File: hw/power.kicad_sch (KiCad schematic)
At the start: 22 parts, among them J2 USB_C_Receptacle_USB2.0_16P, J3 Conn_01x02_Pin, U3 TPD2EUSB30A, U4 BQ24075RGT, U5 TPS63020DSJR

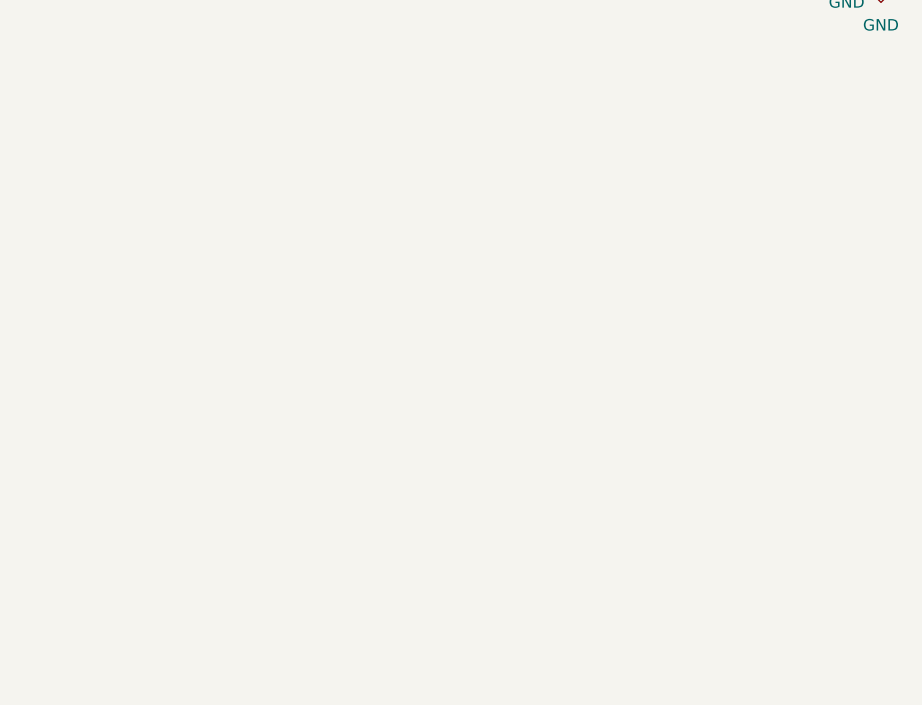
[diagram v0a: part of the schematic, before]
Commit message: added setup files for display and haptics integration
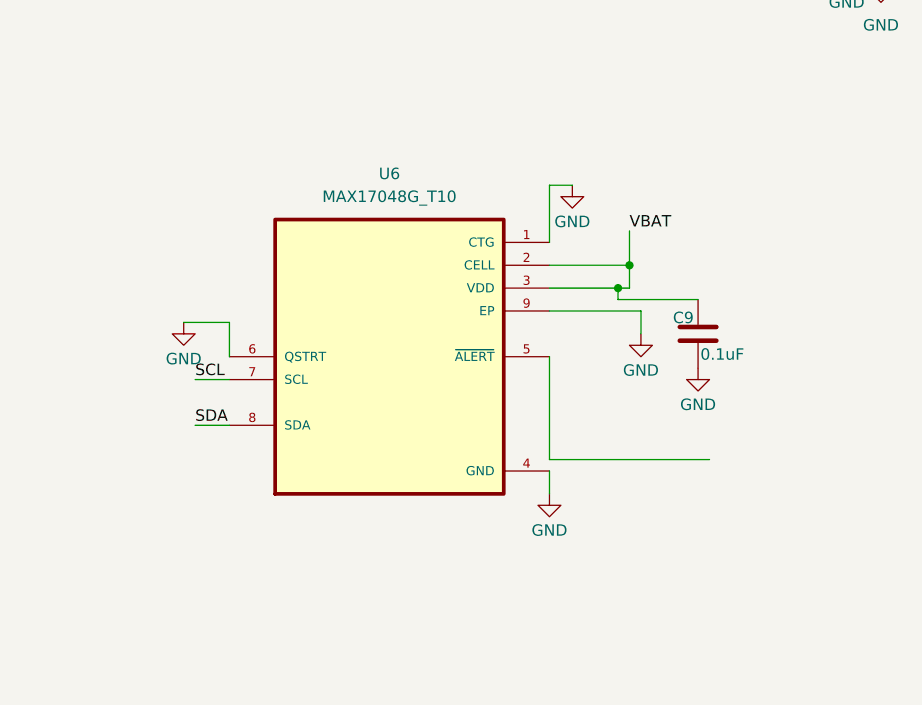
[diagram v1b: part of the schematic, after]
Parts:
- added C9: 0.1uF, symbol Device:C
- added U6: MAX17048G_T10, MAX17048G_T10:SON50P200X200X80-9N, symbol MAX17048G_T10:MAX17048G_T10
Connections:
- net GND: now also C9.1, U6.1 (CTG), U6.4 (GND), U6.6 (QSTRT), U6.9 (EP)
- net VBAT: now also C9.2, U6.2 (CELL), U6.3 (VDD)
- new net SCL: U6.7 (SCL)
- new net SDA: U6.8 (SDA)
